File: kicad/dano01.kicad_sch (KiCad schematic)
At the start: 100 parts, among them J1 1735265-8, J2 1735265-8, SW1 SW_Push, SW10 SW_Push, SW11 SW_Push, SW12 SW_Push, SW13 SW_Push, SW14 SW_Push, SW15 SW_Push, SW16 SW_Push, SW17 SW_Push, SW18 SW_Push, SW19 SW_Push, SW2 SW_Push, SW20 SW_Push, SW21 SW_Push, SW22 SW_Push, SW23 SW_Push, SW24 SW_Push, SW25 SW_Push, SW26 SW_Push, SW27 SW_Push, SW28 SW_Push, SW29 SW_Push, SW3 SW_Push, SW30 SW_Push, SW31 SW_Push, SW32 SW_Push, SW33 SW_Push, SW34 SW_Push, SW35 SW_Push, SW36 SW_Push, SW37 SW_Push, SW38 SW_Push, SW39 SW_Push, SW4 SW_Push, SW40 SW_Push, SW41 SW_Push, SW42 SW_Push, SW43 SW_Push, SW44 SW_Push, SW45 SW_Push, SW46 SW_Push, SW47 SW_Push, SW48 SW_Push, SW49 SW_Push, SW5 SW_Push, SW6 SW_Push, SW7 SW_Push, SW8 SW_Push, SW9 SW_Push

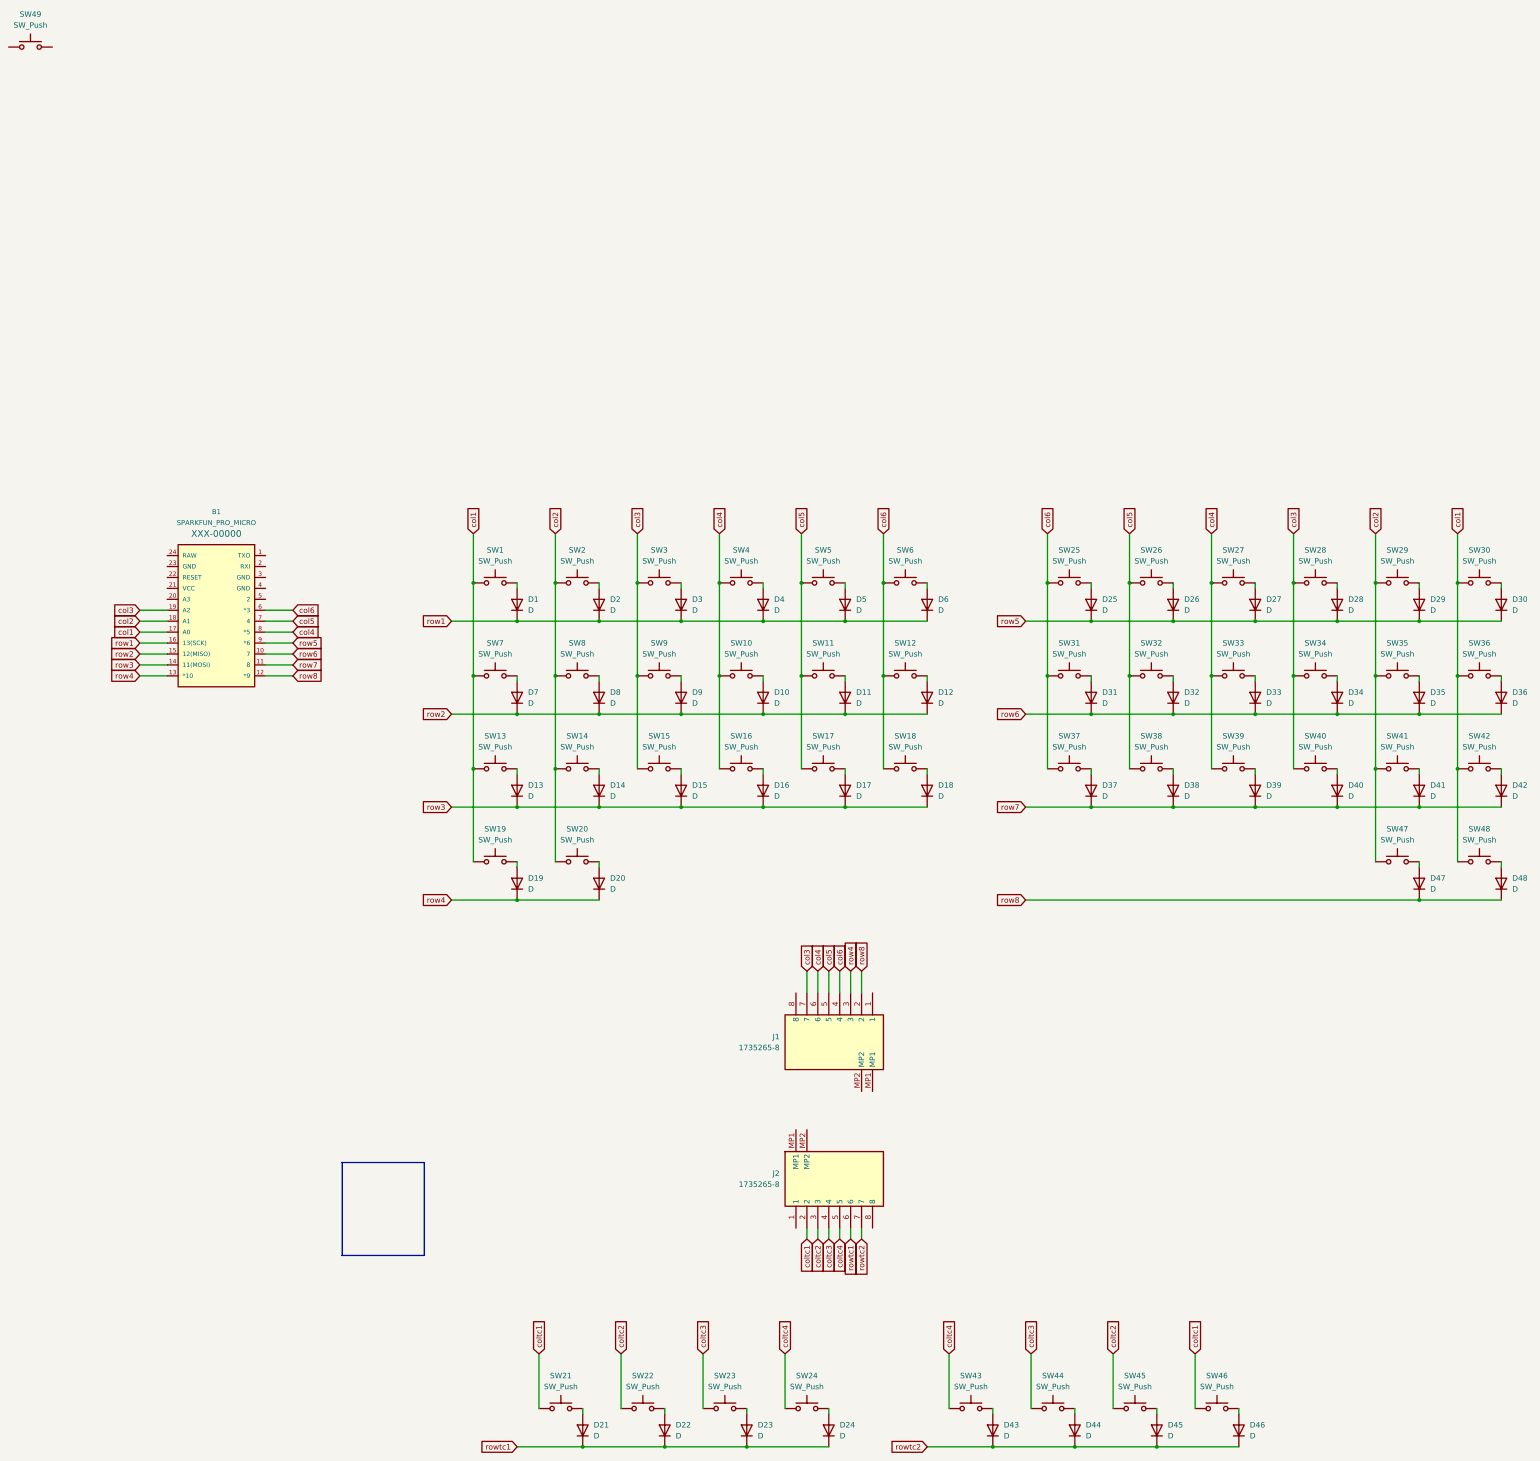
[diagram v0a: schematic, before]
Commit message: kicadでPCB配線までやった。 FFCコネクタの位置を修正する必要あり。
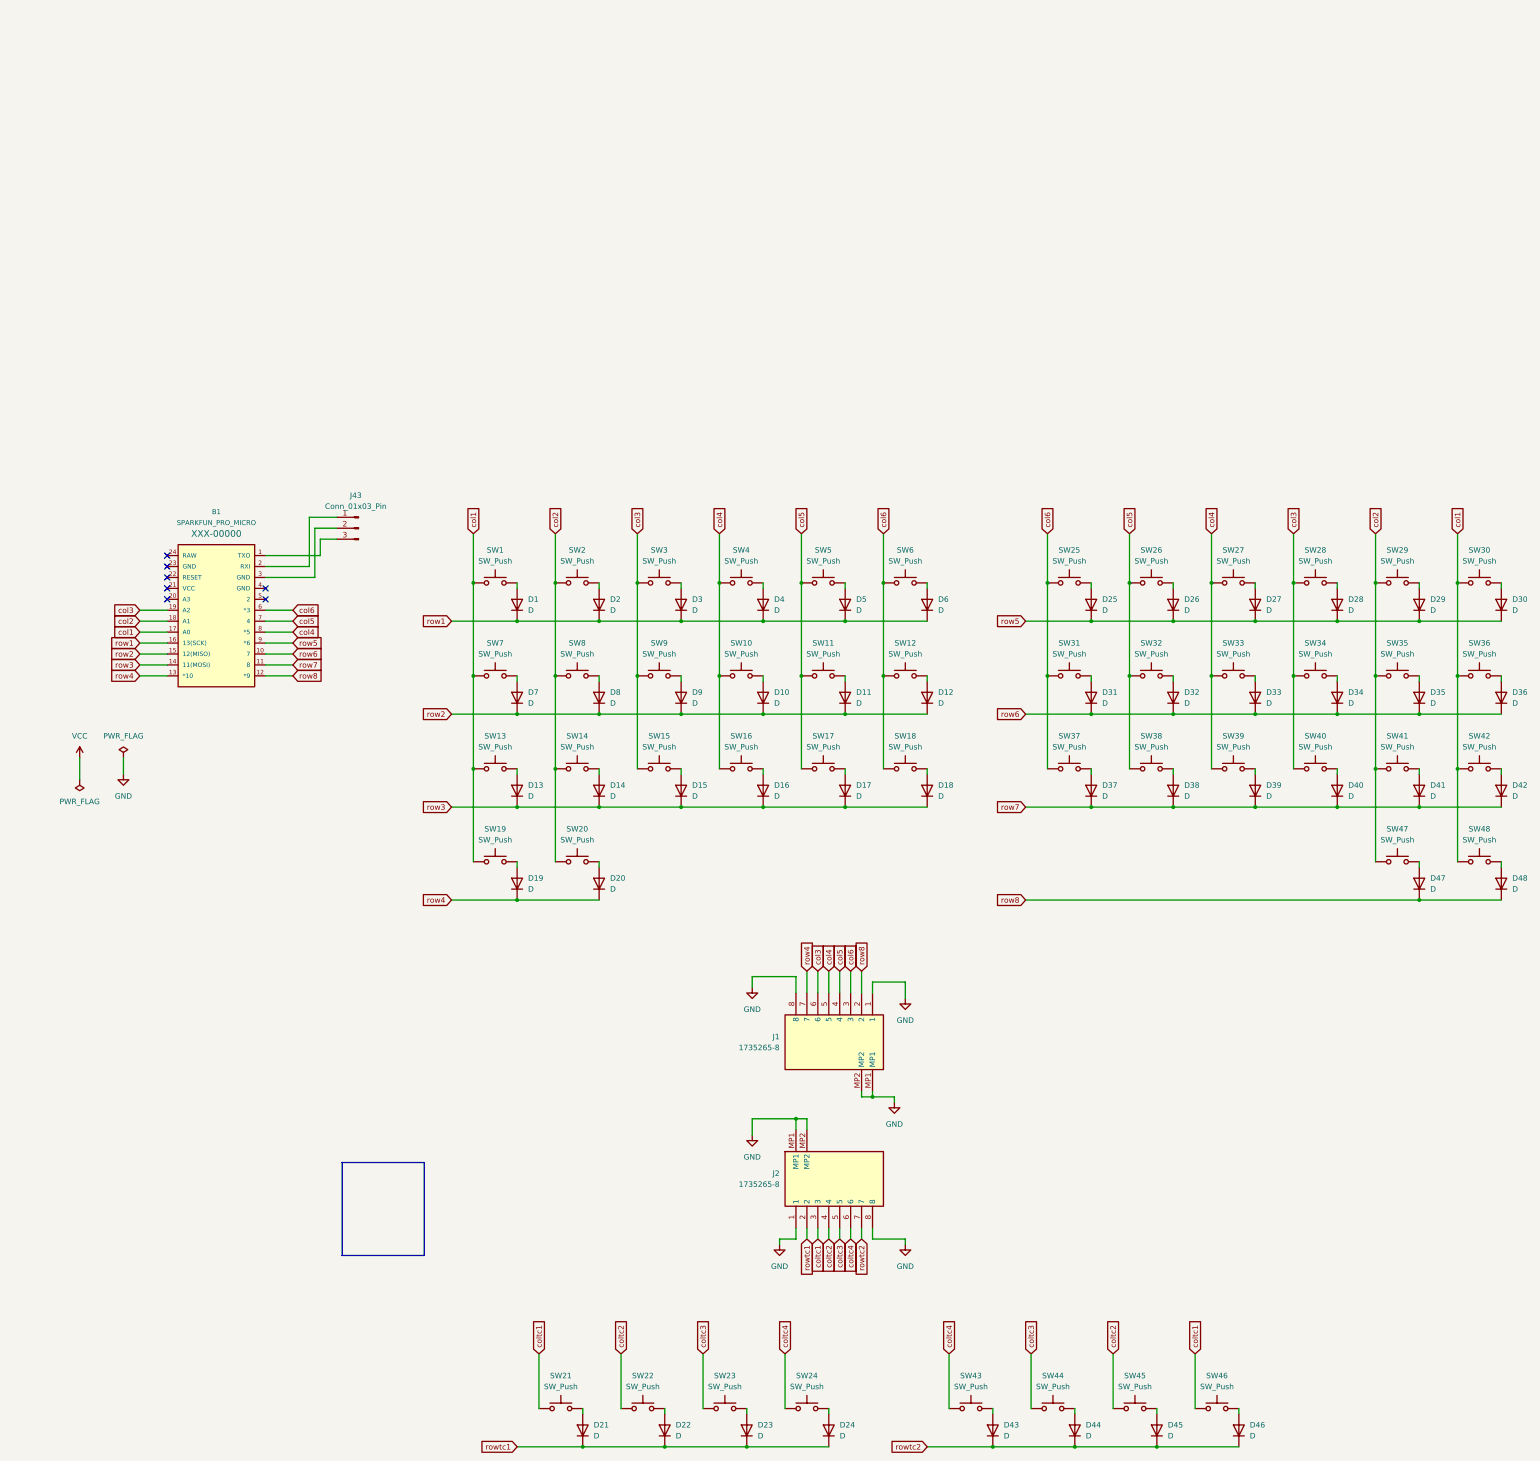
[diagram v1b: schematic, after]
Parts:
- removed SW49: SW_Push, symbol Switch:SW_Push
- added J43: Conn_01x03_Pin, Connector_PinHeader_2.54mm:PinHeader_1x03_P2.54mm_Vertical, symbol Connector:Conn_01x03_Pin
- B1: symbol SparkFun-Boards:SPARKFUN_PRO_MICRO -> pro_micro_rp2040:SPARKFUN_PRO_MICRO
- D1, D10, D11, D12, D13, D14, D15, D16, D17, D18, D19, D2, D20, D21, D22, D23, D24, D25, D26, D27, D28, D29, D3, D30, D31, D32, D33, D34, D35, D36, D37, D38, D39, D4, D40, D41, D42, D43, D44, D45, D46, D47, D48, D5, D6, D7, D8, D9: footprint (none) -> kbd:D3_TH
- SW1, SW10, SW11, SW12, SW13, SW14, SW15, SW16, SW17, SW18, SW19, SW2, SW20, SW21, SW22, SW23, SW24, SW25, SW26, SW27, SW28, SW29, SW3, SW30, SW31, SW32, SW33, SW34, SW35, SW36, SW37, SW38, SW39, SW4, SW40, SW41, SW42, SW43, SW44, SW45, SW46, SW47, SW48, SW5, SW6, SW7, SW8, SW9: footprint (none) -> hernianlib:Kailh_socket_MX
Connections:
- net col3: now also J1.6; no longer J1.7
- net col4: now also J1.5; no longer J1.6
- net col5: now also J1.4; no longer J1.5
- net col6: now also J1.3; no longer J1.4
- net coltc1: now also J2.3; no longer J2.2
- net coltc2: now also J2.4; no longer J2.3
- net coltc3: now also J2.5; no longer J2.4
- net coltc4: now also J2.6; no longer J2.5
- net row4: now also J1.7; no longer J1.3
- net rowtc1: now also J2.2; no longer J2.6
- net at B1.1 (TXO): now also J43.3 (Pin_3)
- net at B1.2 (RXI): now also J43.1 (Pin_1)
- net at B1.3 (GND): now also J43.2 (Pin_2)
- net GND: now reaches J2.1
- net GND: now also J1.1, J1.8, J1.MP1, J1.MP2, J2.8, J2.MP1, J2.MP2
- no-connect marks 0 -> 7

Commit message: Ver. 1.1の発注版
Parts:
- added RSW1: SW_Push, kbd:ResetSW_1side, symbol Switch:SW_Push
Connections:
- net at B1.22 (RESET): now also RSW1.1
- net at B1.23 (GND): now also RSW1.2
- no-connect marks 7 -> 5
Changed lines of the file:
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@@
   (junction (at 317.5 55.88) (diameter 0) (color 0 0 0 0)
   )
-  (no_connect (at 45.72 43.18))
   (no_connect (at 45.72 40.64))
-  (no_connect (at 45.72 45.72))
   (no_connect (at 68.58 48.26))
   (no_connect (at 45.72 50.8))
@@
     (stroke (width 0) (type default))
   )
+  (wire (pts (xy 26.67 43.18) (xy 26.67 45.72))
+    (stroke (width 0) (type default))
+  )
   (wire (pts (xy 127 99.06) (xy 146.05 99.06))
     (stroke (width 0) (type default))
@@
     (stroke (width 0) (type default))
   )
+  (wire (pts (xy 36.83 43.18) (xy 45.72 43.18))
+    (stroke (width 0) (type default))
+  )
   (wire (pts (xy 326.39 90.17) (xy 326.39 111.76))
     (stroke (width 0) (type default))
@@
   )
   (wire (pts (xy 209.55 165.1) (xy 209.55 166.37))
+    (stroke (width 0) (type default))
+  )
+  (wire (pts (xy 45.72 45.72) (xy 26.67 45.72))
     (stroke (width 0) (type default))
   )
@@
         )
       )
+    )
+  )
+  (symbol (lib_id "Switch:SW_Push") (at 31.75 43.18 0) (unit 1)
+    (in_bom yes) (on_board yes) (dnp no) (fields_autoplaced)
+    (property "Reference" "RSW1" (at 31.75 35.56 0)
+      (effects (font (size 1.27 1.27)))
+    )
+    (property "Value" "SW_Push" (at 31.75 38.1 0)
+      (effects (font (size 1.27 1.27)))
+    )
+    (property "Footprint" "kbd:ResetSW_1side" (at 31.75 38.1 0)
+      (effects (font (size 1.27 1.27)) hide)
+    )
+    (property "Datasheet" "~" (at 31.75 38.1 0)
+      (effects (font (size 1.27 1.27)) hide)
+    )
+    (pin "1")
+    (pin "2")
+    (instances
+      (project "dano01"
+        (path "/cb41bcde-3cdf-4c2a-b8db-5b51f32cb34f"
+          (reference "RSW1") (unit 1)
+        )
+      )
